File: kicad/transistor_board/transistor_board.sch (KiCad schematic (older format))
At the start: 18 parts, among them J1 Conn_01x10, J2 Conn_01x02, Q1 MMBF170, Q2 MMBF170, Q3 MMBF170, Q4 MMBF170, U2 ESP32-cam, U3 LM7805_TO220

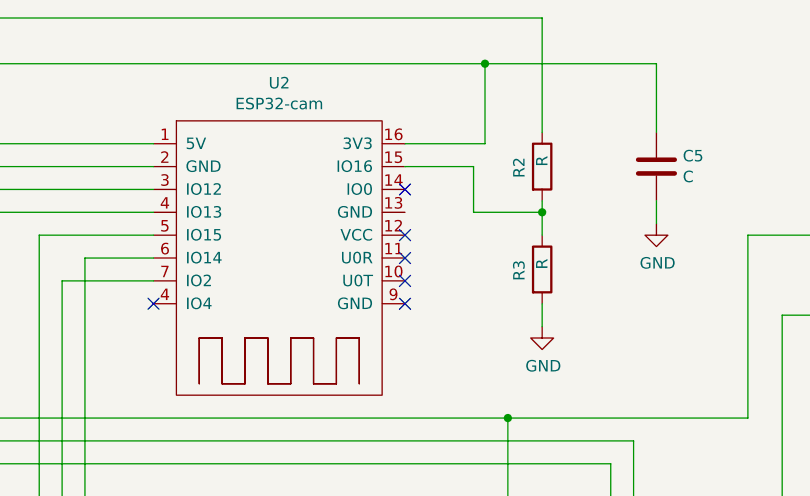
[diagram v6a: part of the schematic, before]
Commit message: Working on bigger transistors
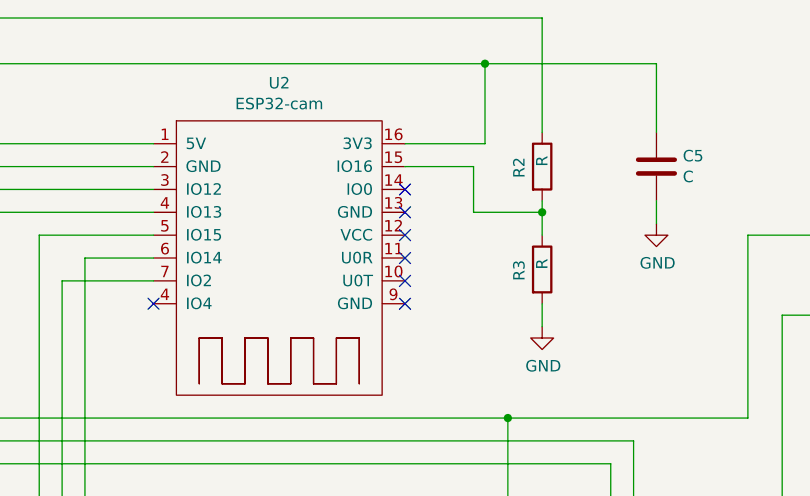
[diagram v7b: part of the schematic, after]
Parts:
- C3, C4, C5, C6: footprint Capacitor_SMD:C_0805_2012Metric -> Capacitor_SMD:C_0805_2012Metric_Pad1.15x1.40mm_HandSolder
- R2, R3: footprint Resistor_SMD:R_0805_2012Metric -> Resistor_SMD:R_0805_2012Metric_Pad1.15x1.40mm_HandSolder
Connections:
- net at U2.4 (IO4): now also Q2.1 (G)
- no-connect marks 6 -> 7
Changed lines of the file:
@@
 F 0 "C4" H 5265 1146 50  0000 L CNN
 F 1 "C" H 5265 1055 50  0000 L CNN
-F 2 "Capacitor_SMD:C_0805_2012Metric" H 5188 950 50  0001 C CNN
+F 2 "Capacitor_SMD:C_0805_2012Metric_Pad1.15x1.40mm_HandSolder" H 5188 950 50  0001 C CNN
 F 3 "~" H 5150 1100 50  0001 C CNN
 	1    5150 1100
@@
 F 0 "C5" H 8915 1196 50  0000 L CNN
 F 1 "C" H 8915 1105 50  0000 L CNN
-F 2 "Capacitor_SMD:C_0805_2012Metric" H 8838 1000 50  0001 C CNN
+F 2 "Capacitor_SMD:C_0805_2012Metric_Pad1.15x1.40mm_HandSolder" H 8838 1000 50  0001 C CNN
 F 3 "~" H 8800 1150 50  0001 C CNN
 	1    8800 1150
@@
 F 0 "C3" V 4750 1950 50  0000 C CNN
 F 1 "C" V 5050 1950 50  0000 C CNN
-F 2 "Capacitor_SMD:C_0805_2012Metric" H 4938 1800 50  0001 C CNN
+F 2 "Capacitor_SMD:C_0805_2012Metric_Pad1.15x1.40mm_HandSolder" H 4938 1800 50  0001 C CNN
 F 3 "~" H 4900 1950 50  0001 C CNN
 	1    4900 1950
@@
 F 0 "C6" V 3398 1050 50  0000 C CNN
 F 1 "C" V 3489 1050 50  0000 C CNN
-F 2 "Capacitor_SMD:C_0805_2012Metric" H 3688 900 50  0001 C CNN
+F 2 "Capacitor_SMD:C_0805_2012Metric_Pad1.15x1.40mm_HandSolder" H 3688 900 50  0001 C CNN
 F 3 "~" H 3650 1050 50  0001 C CNN
 	1    3650 1050
@@
 F 0 "R3" V 8200 1550 50  0000 L CNN
 F 1 "R" V 8300 1600 50  0000 L CNN
-F 2 "Resistor_SMD:R_0805_2012Metric" V 8230 1600 50  0001 C CNN
+F 2 "Resistor_SMD:R_0805_2012Metric_Pad1.15x1.40mm_HandSolder" V 8230 1600 50  0001 C CNN
 F 3 "~" H 8300 1600 50  0001 C CNN
 	1    8300 1600
@@
 F 0 "R2" V 8200 1100 50  0000 L CNN
 F 1 "R" V 8300 1150 50  0000 L CNN
-F 2 "Resistor_SMD:R_0805_2012Metric" V 8230 1150 50  0001 C CNN
+F 2 "Resistor_SMD:R_0805_2012Metric_Pad1.15x1.40mm_HandSolder" V 8230 1150 50  0001 C CNN
 F 3 "~" H 8300 1150 50  0001 C CNN
 	1    8300 1150
@@
 Wire Wire Line
 	8300 500  8300 1000
+NoConn ~ 7700 1350
 $EndSCHEMATC

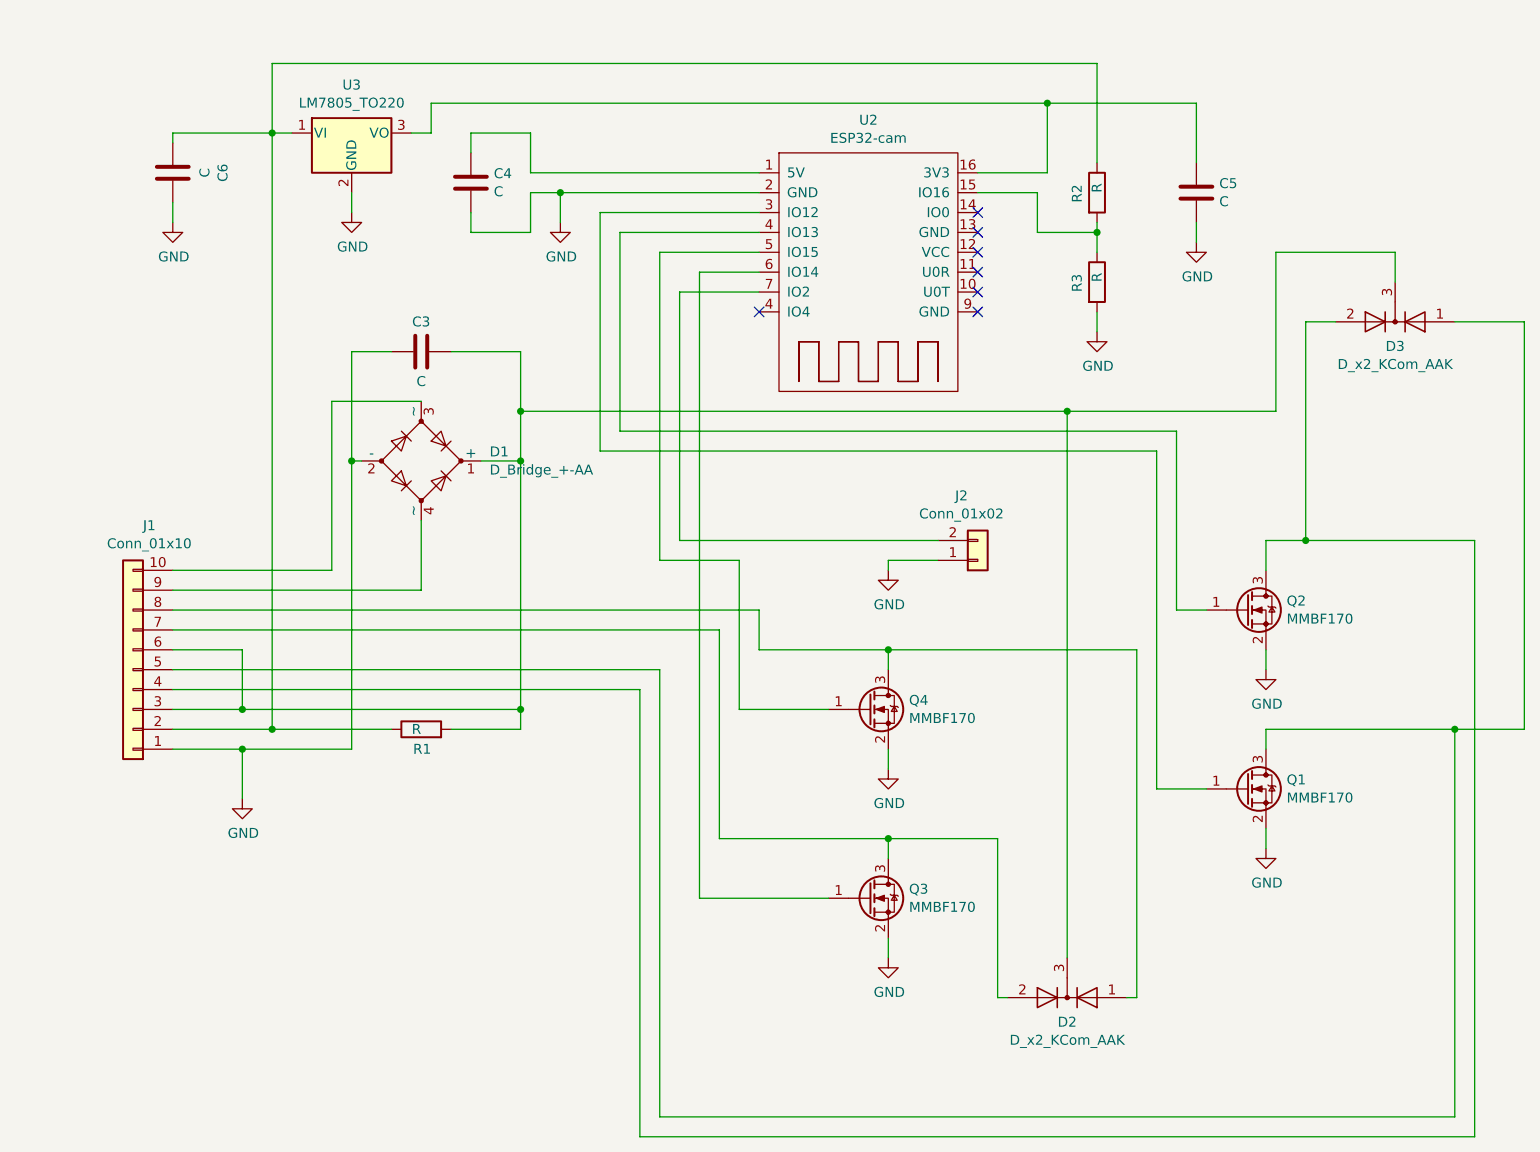
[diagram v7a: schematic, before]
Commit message: Working on bigger transistors
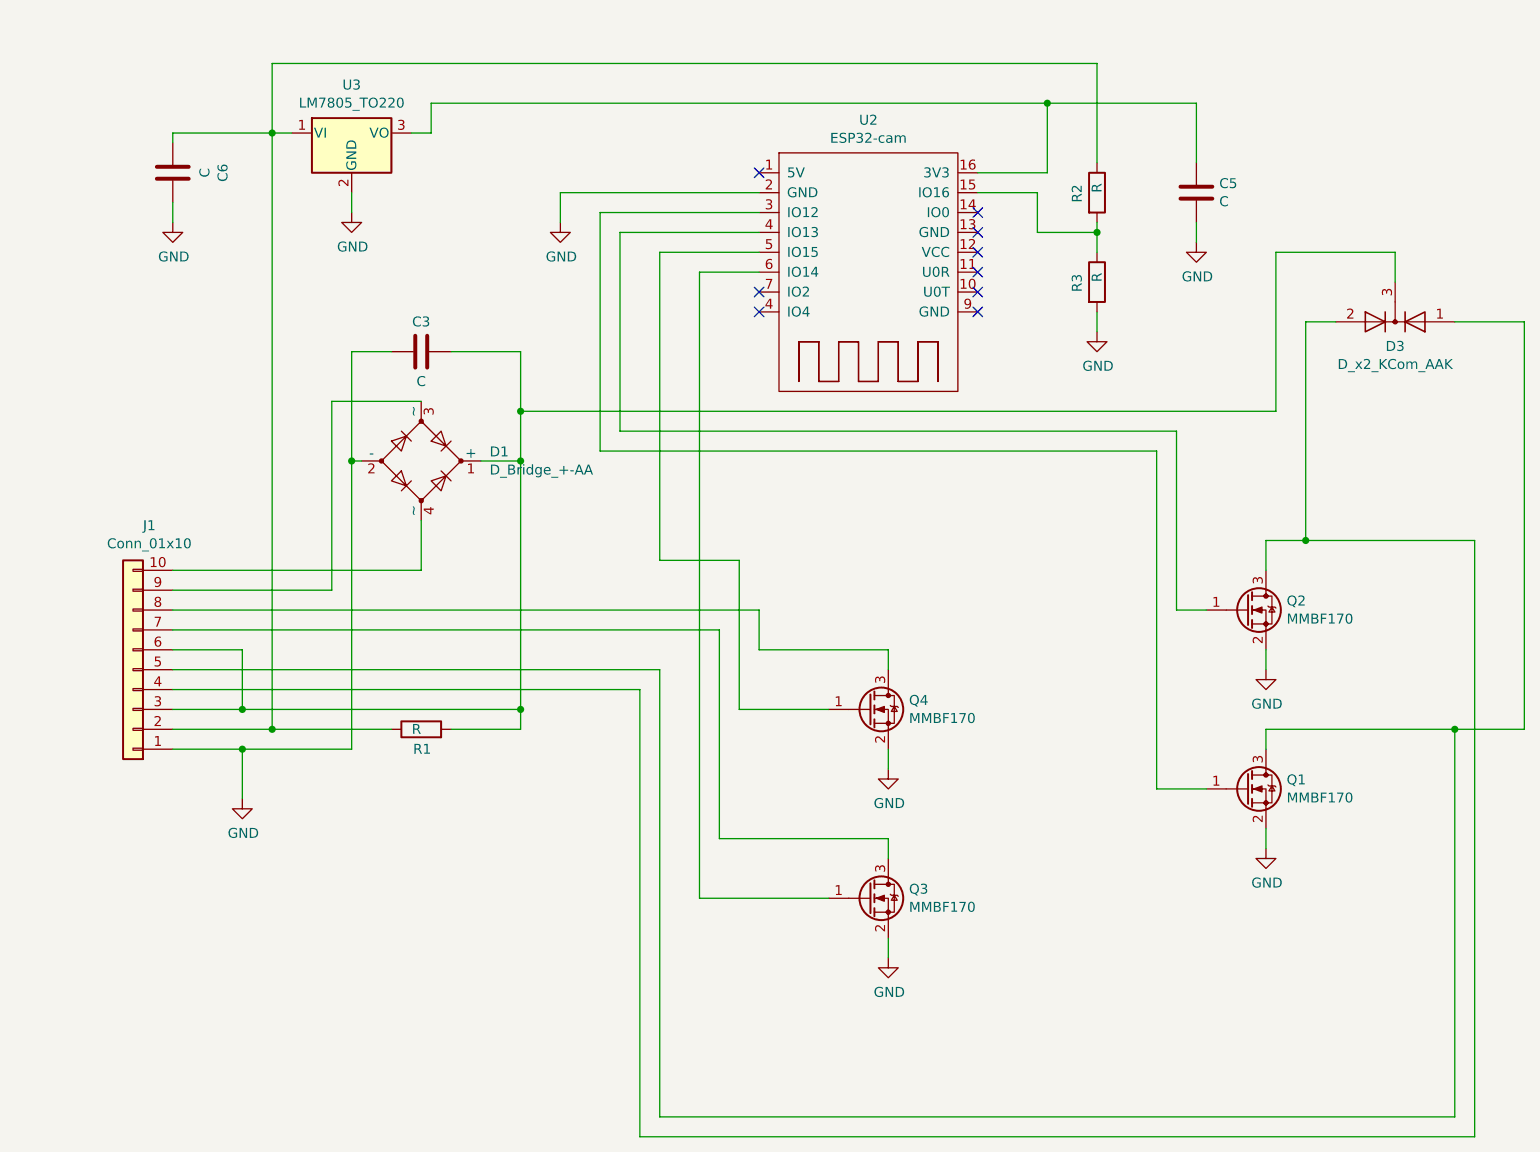
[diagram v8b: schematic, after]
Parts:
- removed C4: C, Capacitor_SMD:C_0805_2012Metric_Pad1.15x1.40mm_HandSolder, symbol transistor_board-rescue:C-Device
- removed D2: D_x2_KCom_AAK, digikey-footprints:SOT-23-3, symbol transistor_board-rescue:D_x2_KCom_AAK-Device
- removed J2: Conn_01x02, Connector_PinHeader_2.54mm:PinHeader_1x02_P2.54mm_Vertical, symbol transistor_board-rescue:Conn_01x02-Connector_Generic
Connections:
- net at U2.4 (IO4): now also Q2.1 (G)
- net at D1.3 (~~): now also J1.9 (Pin_9); no longer J1.10 (Pin_10)
- net at D1.4 (~~): now also J1.10 (Pin_10); no longer J1.9 (Pin_9)
- no-connect marks 7 -> 9
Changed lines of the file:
@@
 Sheet 1 1
 Title ""
-Date "2020-09-15"
+Date "2020-09-30"
 Rev ""
 Comp ""
@@
 	4450 2200 4900 2200
 Wire Wire Line
-	4900 2800 4900 3150
+	4900 2800 4900 3050
 Wire Wire Line
 	4600 2500 4550 2500
@@
 	5600 1150 6600 1150
 $Comp
-L transistor_board-rescue:C-Device C4
-U 1 1 5F2E553A
-P 5150 1100
-F 0 "C4" H 5265 1146 50  0000 L CNN
-F 1 "C" H 5265 1055 50  0000 L CNN
-F 2 "Capacitor_SMD:C_0805_2012Metric_Pad1.15x1.40mm_HandSolder" H 5188 950 50  0001 C CNN
-F 3 "~" H 5150 1100 50  0001 C CNN
-	1    5150 1100
-	1    0    0    -1
-$EndComp
-Wire Wire Line
-	5600 1150 5450 1150
-Wire Wire Line
-	5450 1150 5450 1350
-Wire Wire Line
-	5450 1350 5150 1350
-Wire Wire Line
-	5150 1350 5150 1250
-Connection ~ 5600 1150
-Wire Wire Line
-	5150 950  5150 850
-Wire Wire Line
-	5150 850  5450 850
-Wire Wire Line
-	5450 850  5450 1050
-Wire Wire Line
-	5450 1050 6600 1050
-$Comp
 L transistor_board-rescue:LM7805_TO220-Regulator_Linear U3
 U 1 1 5F300908
@@
 	5400 3750 5400 3850
 Wire Wire Line
-	3650 3050 4450 3050
-Wire Wire Line
-	4450 2200 4450 3050
-Wire Wire Line
-	3650 3150 4900 3150
-Wire Wire Line
 	3650 3250 6600 3250
 Wire Wire Line
@@
 $EndComp
 Wire Wire Line
-	5400 2250 8150 2250
-Wire Wire Line
 	9800 1600 9800 1450
 Wire Wire Line
@@
 Wire Wire Line
 	9350 2900 10200 2900
-$Comp
-L transistor_board-rescue:D_x2_KCom_AAK-Device D2
-U 1 1 5F29965A
-P 8150 5200
-F 0 "D2" H 8150 5323 50  0000 C CNN
-F 1 "D_x2_KCom_AAK" H 8150 5414 50  0000 C CNN
-F 2 "digikey-footprints:SOT-23-3" H 8150 5200 50  0001 C CNN
-F 3 "~" H 8150 5200 50  0001 C CNN
-	1    8150 5200
-	-1   0    0    1
-$EndComp
-Wire Wire Line
-	8150 5000 8150 2250
-Connection ~ 8150 2250
-Wire Wire Line
-	8150 2250 9200 2250
-Wire Wire Line
-	7250 4400 7800 4400
-Wire Wire Line
-	7800 4400 7800 5200
-Wire Wire Line
-	7800 5200 7850 5200
-Connection ~ 7250 4400
-Wire Wire Line
-	7250 3450 8500 3450
-Connection ~ 7250 3450
-Wire Wire Line
-	8500 5200 8450 5200
-Wire Wire Line
-	8500 3450 8500 5200
 NoConn ~ 6600 1750
 NoConn ~ 7700 1450
@@
 NoConn ~ 7700 1650
 NoConn ~ 7700 1750
-Wire Wire Line
-	6600 1650 6200 1650
-Wire Wire Line
-	6200 2900 6200 1650
-Wire Wire Line
-	6200 2900 7500 2900
-Wire Wire Line
-	7250 3000 7250 3050
-Wire Wire Line
-	7500 3000 7250 3000
-$Comp
-L transistor_board-rescue:Conn_01x02-Connector_Generic J2
-U 1 1 5F30B63D
-P 7700 3000
-F 0 "J2" H 7618 2675 50  0000 C CNN
-F 1 "Conn_01x02" H 7618 2766 50  0000 C CNN
-F 2 "Connector_PinHeader_2.54mm:PinHeader_1x02_P2.54mm_Vertical" H 7700 3000 50  0001 C CNN
-F 3 "~" H 7700 3000 50  0001 C CNN
-	1    7700 3000
-	1    0    0    1
-$EndComp
-$Comp
-L transistor_board-rescue:GND-power #PWR06
-U 1 1 5F260D53
-P 7250 3050
-F 0 "#PWR06" H 7250 2800 50  0001 C CNN
-F 1 "GND" H 7255 2877 50  0000 C CNN
-F 2 "" H 7250 3050 50  0001 C CNN
-F 3 "" H 7250 3050 50  0001 C CNN
-	1    7250 3050
-	1    0    0    -1
-$EndComp
 NoConn ~ 7700 1250
 $Comp
@@
 	8300 500  8300 1000
 NoConn ~ 7700 1350
+Wire Wire Line
+	4450 3150 3650 3150
+Wire Wire Line
+	4450 2200 4450 3150
+Wire Wire Line
+	3650 3050 4900 3050
+NoConn ~ 6600 1650
+Wire Wire Line
+	5400 2250 9200 2250
+NoConn ~ 6600 1050
 $EndSCHEMATC
